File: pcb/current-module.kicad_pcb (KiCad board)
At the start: 4 copper layers, 50 x 50 mm, 126 parts, among them J2 SWD Header, SW1 SKRPABE010, U1 STM32C051G8Ux, U2 A1324LLHLT-T, U3 A1324LLHLT-T, U4 TLV9064, Y1 ECS-480-10-37B2-RWN-TR

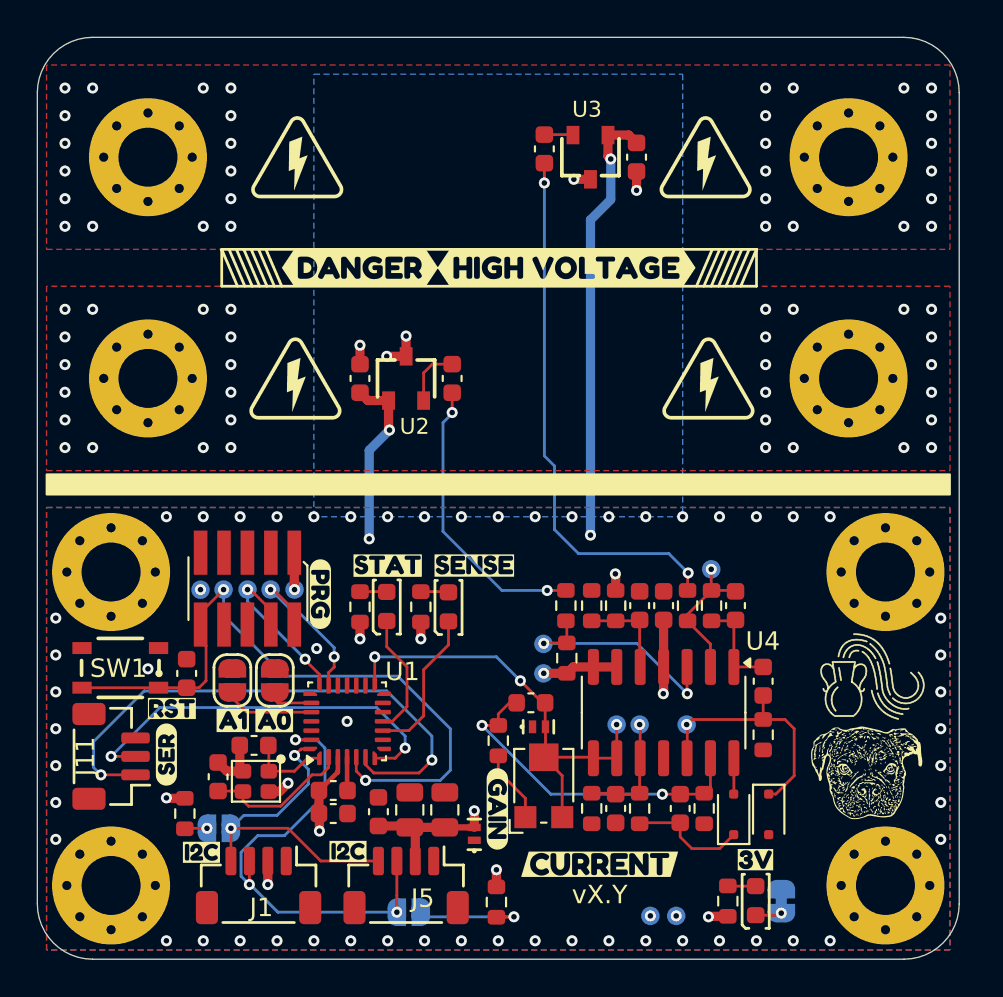
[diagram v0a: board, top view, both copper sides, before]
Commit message: Added additional silkscreen to AC side
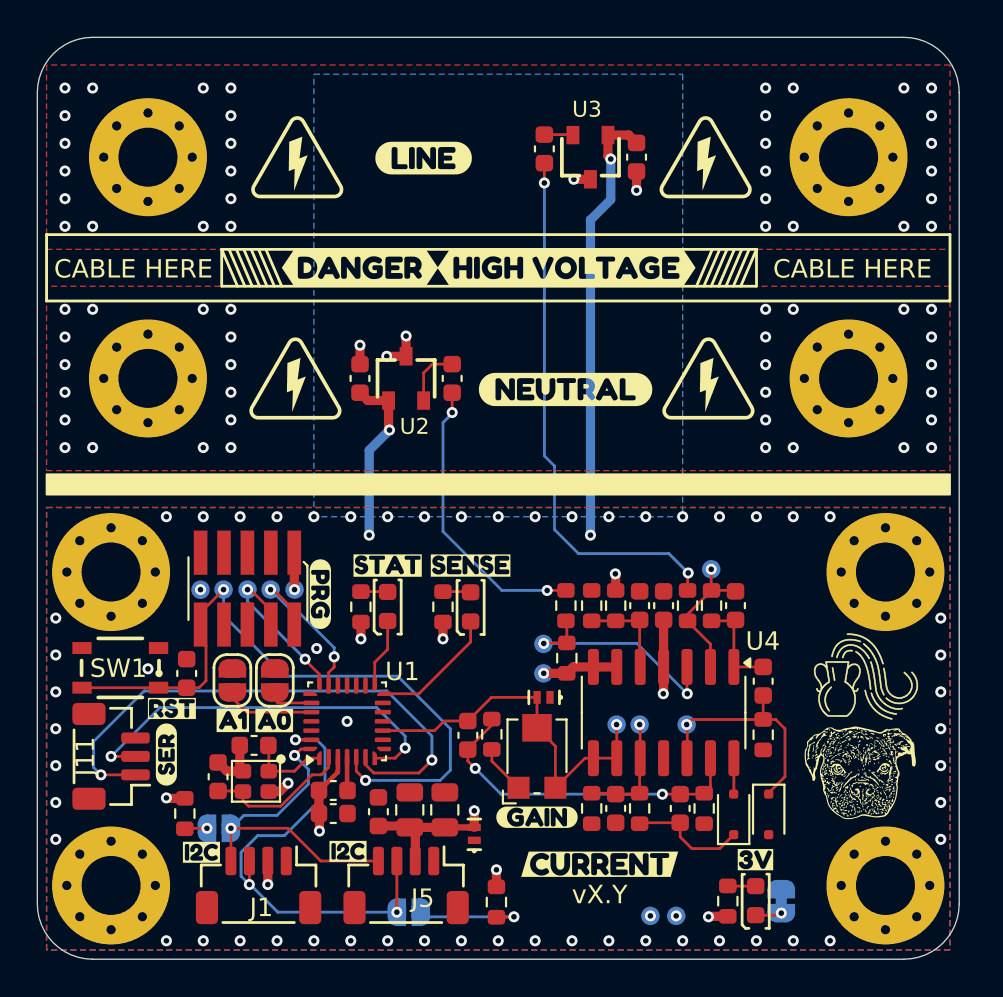
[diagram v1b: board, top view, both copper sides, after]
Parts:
- added kibuzzard-6AA9ECA7: G***, kibuzzard-6AA9ECA7, F.Cu at (71.0, 106.5)
- added kibuzzard-6AA9ECB3: G***, kibuzzard-6AA9ECB3, F.Cu at (78.7, 119.1)
- moved C19 3.84 mm to (73.3, 137.9), turned to 90 degrees
- moved kibuzzard-6AA87574 2.20 mm to (77.1, 142.3), turned to 0 degrees
- moved RV1 1.64 mm to (77.1, 138.9)
- moved D12 1.61 mm to (77.5, 135.8), turned to 180 degrees
- moved D1 1.20 mm to (73.5, 130.9)
- moved R3 1.20 mm to (72.0, 130.9)
- moved R19 0.49 mm to (74.7, 137.8)
- moved LOGO5 0.35 mm to (94.7, 139.9)
- moved LOGO7 0.35 mm to (94.7, 135.1)
- moved kibuzzard-6AA87368 0.20 mm to (73.5, 128.7)
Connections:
- U1 pad 10: /MCU/SENSE -> IO1
- U1 pad 11: /MCU/STATUS -> IO2
- U1 pad 12: IO4 -> IO3
- U1 pad 13: IO3 -> IO4
- U1 pad 14: IO2 -> /MCU/SENSE
- U1 pad 15: IO1 -> /MCU/STATUS
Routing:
- net IO1: track 23.9 -> 20.2 mm, vias 3 -> 1
- net /MCU/STATUS: track 6.75 -> 3.74 mm
- net Net-(R19-Pad1): track 3.93 -> 2.68 mm
- net /MCU/SENSE: track 8.23 -> 6.99 mm
- net /Current Sensor/PEAK: track 13.6 -> 12.6 mm
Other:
- board text added: "CABLE HERE"
